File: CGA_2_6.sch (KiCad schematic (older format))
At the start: 11 parts, among them U24 74LS244, U32 74LS166, U33 27C256, U34 74LS273, U35 74LS273, U36 74LS244, U37 74LS374, U39 74LS174, U68 74LS86, U7 74LS166

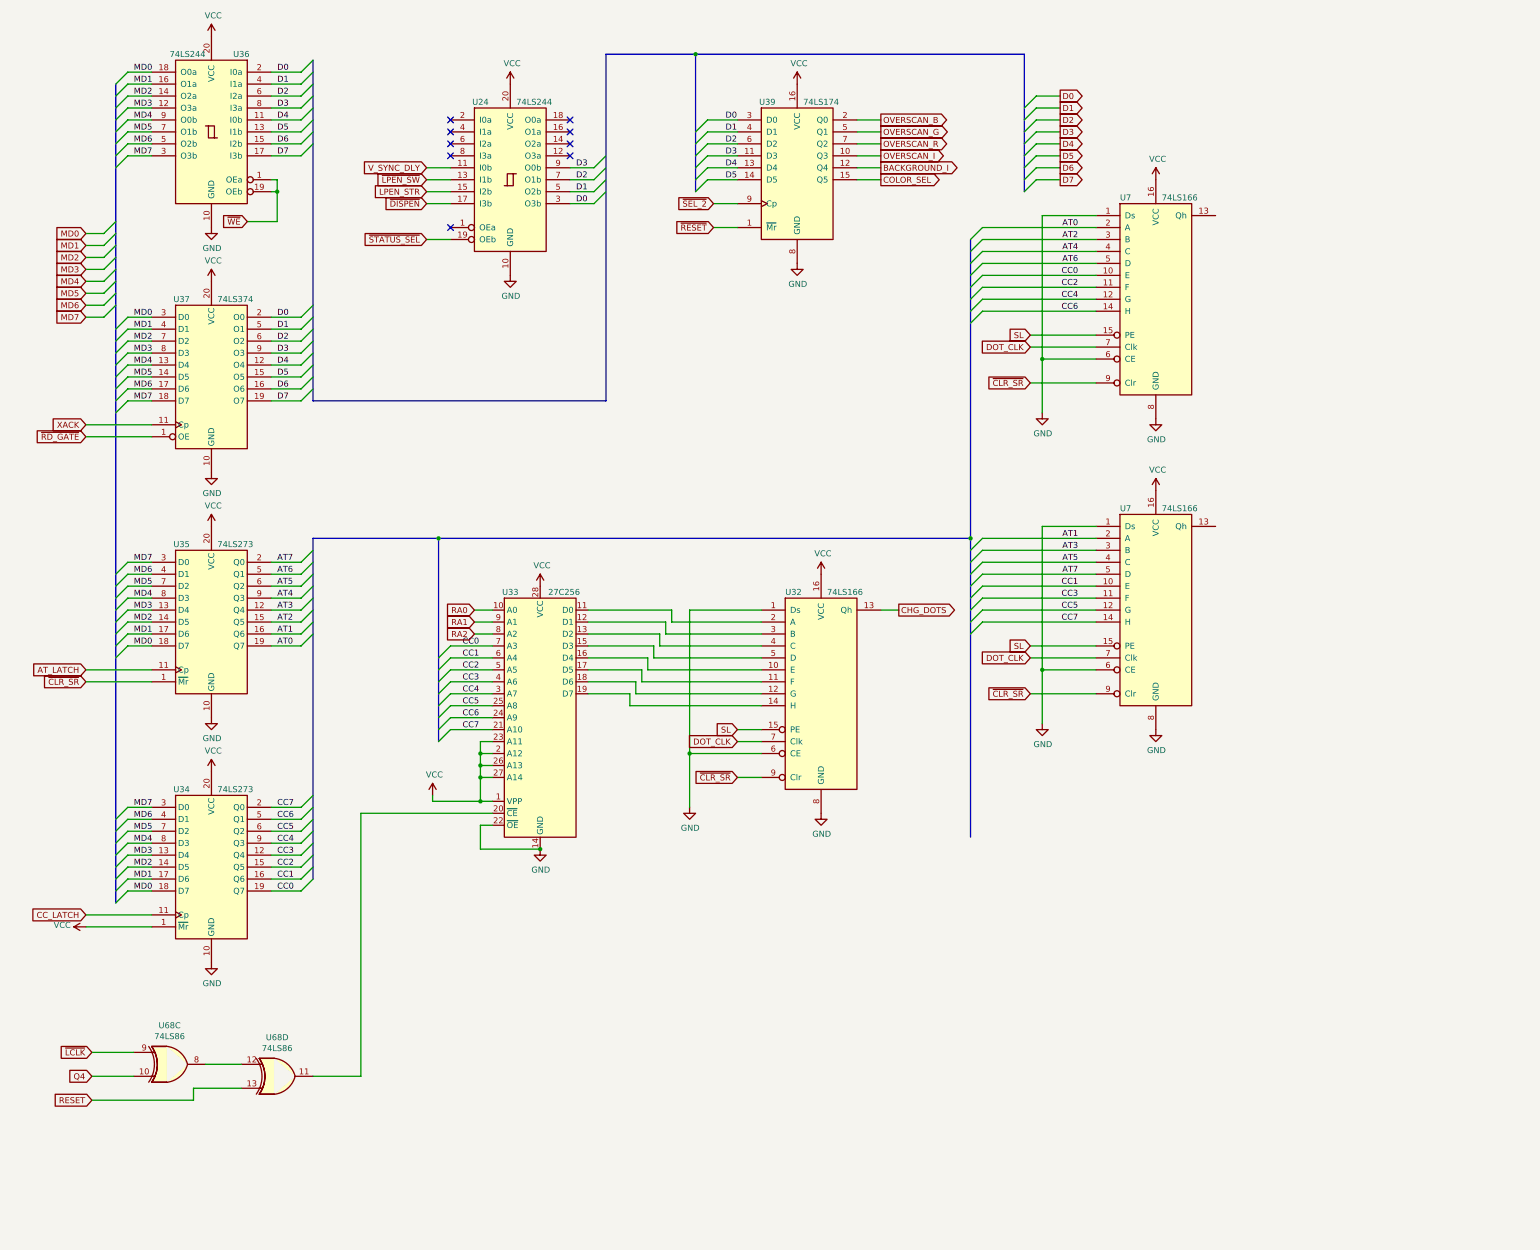
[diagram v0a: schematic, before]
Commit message: More of sheet 2
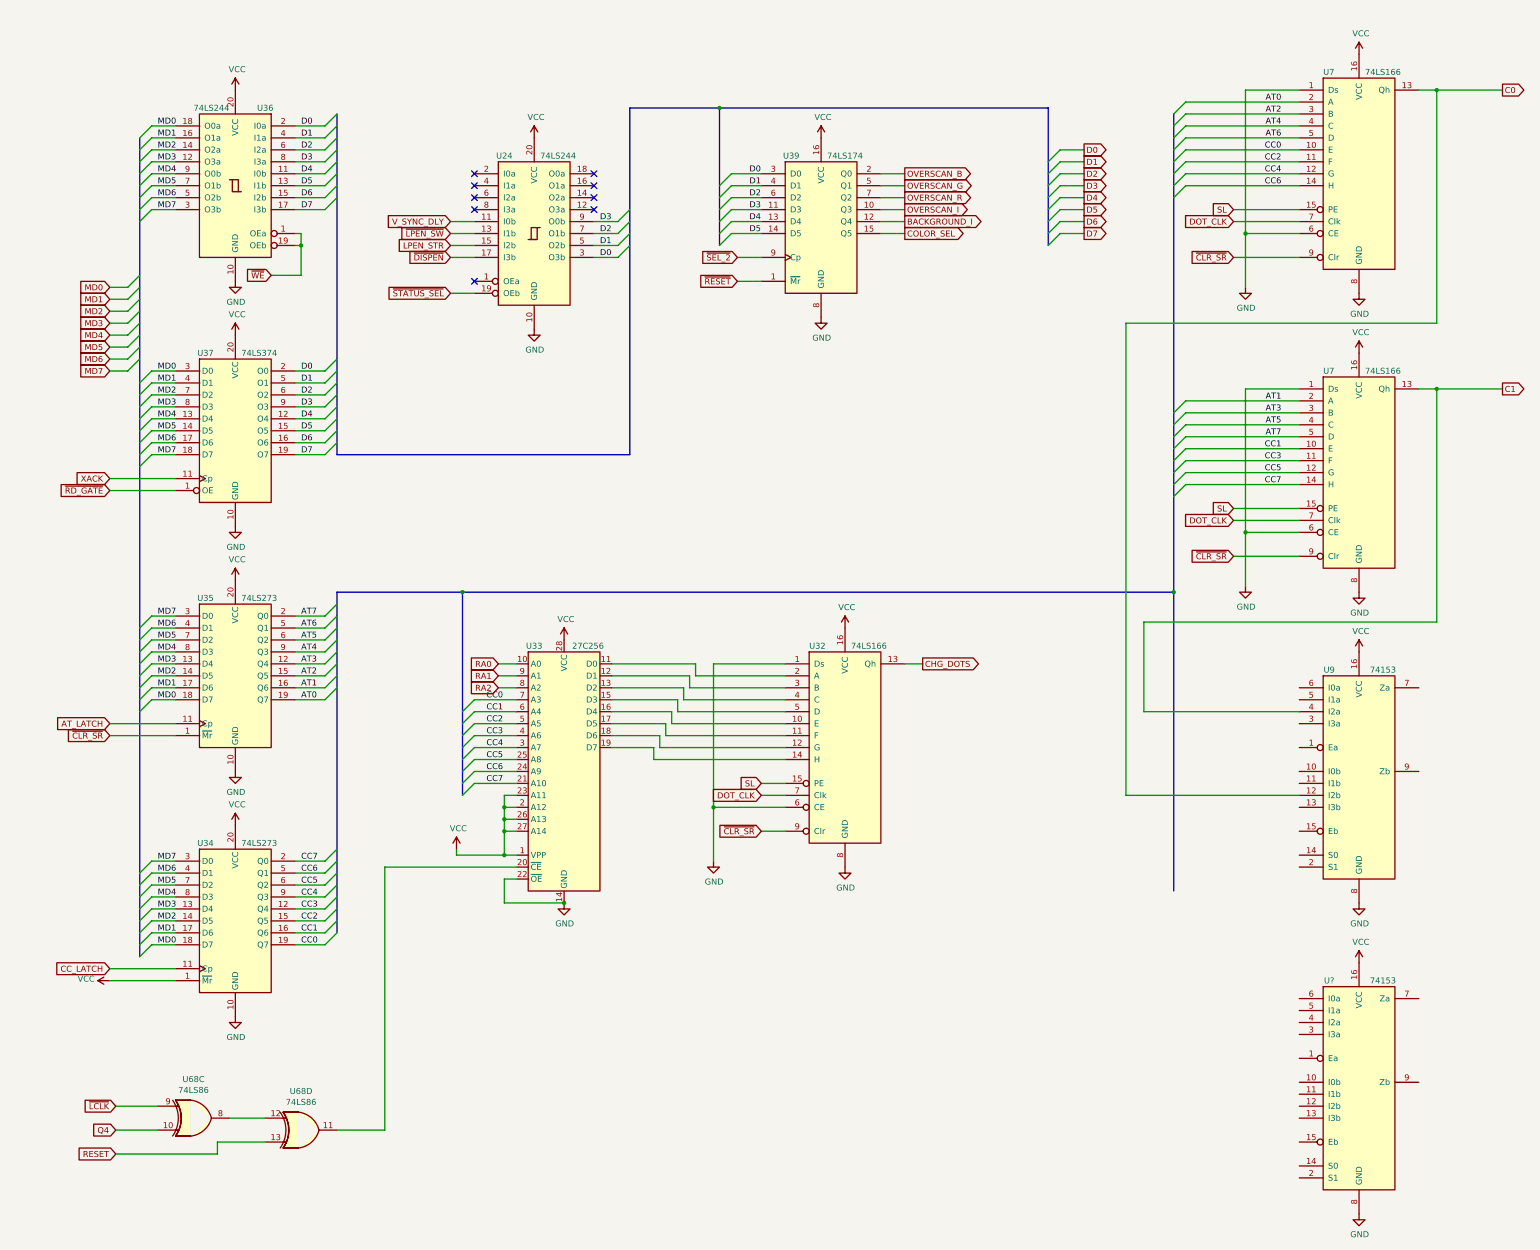
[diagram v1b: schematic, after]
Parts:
- added U9, U?: 74153, Package_DIP:DIP-16_W7.62mm_LongPads, symbol 74xx:74LS153
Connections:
- net GND: now also U9.8 (GND), U?.8 (GND)
- net VCC: now also U9.16 (VCC), U?.16 (VCC)
- net C0: now reaches U7.13 (Qh)
- net C0: now also U9.12 (I2b)
- net C1: now reaches U7.13 (Qh)
- net C1: now also U9.4 (I2a)
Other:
- moved on the sheet: U24, U32, U33, U34, U35, U36, U37, U39, U68C, U68D, U7

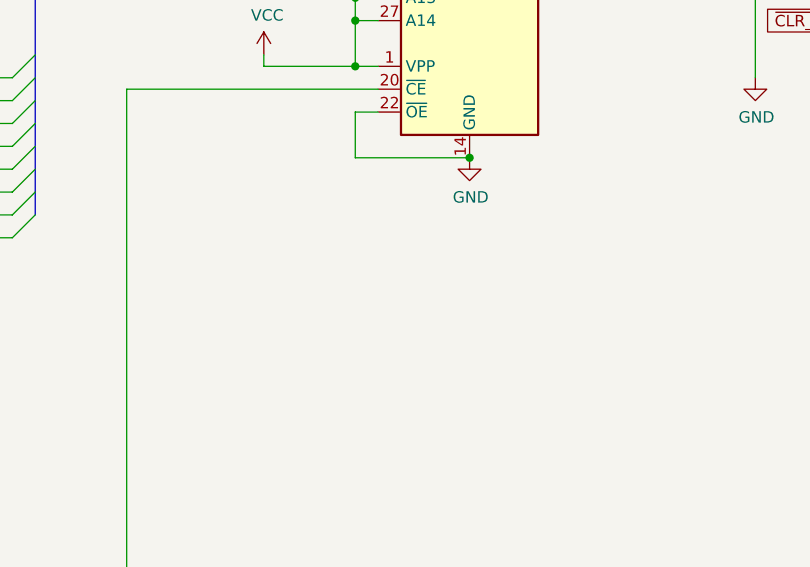
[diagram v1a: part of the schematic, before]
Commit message: Added MK36000 symbol
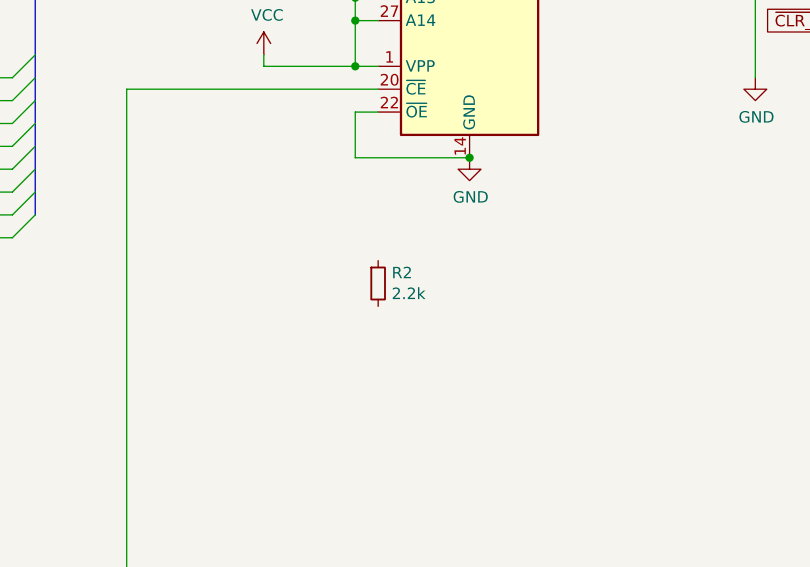
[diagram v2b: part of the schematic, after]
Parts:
- added R2: 2.2k, Resistor_THT:R_Axial_DIN0207_L6.3mm_D2.5mm_P10.16mm_Horizontal, symbol Device:R_Small
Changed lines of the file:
@@
 Wire Wire Line
 	12750 3950 13300 3950
+$Comp
+L Device:R_Small R2
+U 1 1 612D31E2
+P 5050 8800
+F 0 "R2" H 5109 8846 50  0000 L CNN
+F 1 "2.2k" H 5109 8755 50  0000 L CNN
+F 2 "Resistor_THT:R_Axial_DIN0207_L6.3mm_D2.5mm_P10.16mm_Horizontal" H 5050 8800 50  0001 C CNN
+F 3 "~" H 5050 8800 50  0001 C CNN
+	1    5050 8800
+	1    0    0    -1
+$EndComp
 $EndSCHEMATC

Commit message: More sheet 2
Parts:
- removed U33: 27C256, Package_DIP:DIP-28_W15.24mm_LongPads, symbol Memory_EPROM:27C256
- added U31: 74S08, Package_DIP:DIP-14_W7.62mm_LongPads, symbol 74xx:74LS08
- added U33: MK36000, Package_DIP:DIP-24_W15.24mm_LongPads, symbol ISA_CGA:MK36000
- gave numbers to parts that had none: 1
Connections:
- net AT0: now also U10.6 (I0a)
- net AT1: now also U9.10 (I0b)
- net AT2: now also U9.6 (I0a)
- net AT3: now also U10.10 (I0b)
- net AT4: now also U10.5 (I1a)
- net AT5: now also U9.11 (I1b)
- net AT6: now also U9.5 (I1a)
- net AT7: now also U31.9
- net CC0: now also U33.5 (A3)
- net CC1: now also U33.4 (A4)
- net CC2: now also U33.3 (A5)
- net CC3: now also U33.2 (A6)
- net CC4: now also U33.1 (A7)
- net CC5: now also U33.23 (A8)
- net CC6: now also U33.22 (A9)
- net CC7: now also U33.19 (A10)
- net GND: now also U33.12 (GND)
- net OVERSCAN_B: now also U10.3 (I3a)
- net OVERSCAN_G: now also U9.13 (I3b)
- net OVERSCAN_R: now also U9.3 (I3a)
- net RA0: now also U33.8 (A0)
- net RA1: now also U33.7 (A1)
- net RA2: now also U33.6 (A2)
- net VCC: now also R2.2, U33.21 (A12), U33.24 (VCC)
- net at U32.2 (A): now also U33.9 (D0)
- net at U32.3 (B): now also U33.10 (D1)
- net at U32.4 (C): now also U33.11 (D2)
- net at U32.5 (D): now also U33.13 (D3)
- net at U32.10 (E): now also U33.14 (D4)
- net at U32.11 (F): now also U33.15 (D5)
- net at U32.12 (G): now also U33.16 (D6)
- net at U32.14 (H): now also U33.17 (D7)
- net at U68.11: now also U33.20 (~CE)
- net STR: now reaches U9.1 (Ea)
- net STR: now also U10.1 (Ea), U10.15 (Eb), U9.15 (Eb)
- net MUX_A: now reaches U9.14 (S0)
- net MUX_A: now also U10.14 (S0)
- net MUX_B: now reaches U9.2 (S1)
- net MUX_B: now also U10.2 (S1)
- net at U10.11 (I1b): now also U31.8
- net SEL_BLUE: now reaches U10.4 (I2a)
- net at R2.1: now also U33.18 (A11)
- new net ~ENABLE_BLINK: U31.10
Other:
- moved on the sheet: R2

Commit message: More sheet 2
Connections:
- net BACKGROUND_I: now also U10.12 (I2b)
- net OVERSCAN_I: now also U10.13 (I3b)
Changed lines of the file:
@@
 Wire Wire Line
 	8950 9100 8150 9100
+Text GLabel 8150 9100 0    50   Input ~ 0
+~ENABLE_BLINK
+Wire Wire Line
+	11600 9950 10750 9950
+Wire Wire Line
+	10750 9950 10750 10050
+Wire Wire Line
+	10750 10050 9550 10050
+Text GLabel 9550 10050 0    50   Input ~ 0
+BACKGROUND_I
+Wire Wire Line
+	11600 10050 10850 10050
+Wire Wire Line
+	10850 10050 10850 10150
+Wire Wire Line
+	10850 10150 9550 10150
 Wire Bus Line
 	6000 1600 6000 4500
@@
 Wire Bus Line
 	1900 1850 1900 8700
-Text GLabel 8150 9100 0    50   Input ~ 0
-~ENABLE_BLINK
+Text GLabel 9550 10150 0    50   Input ~ 0
+OVERSCAN_I
 $EndSCHEMATC

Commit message: More sheet 2 changes
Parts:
- added U101: 74S174, Package_DIP:DIP-16_W7.62mm_LongPads, symbol 74xx:74LS174
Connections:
- net GND: now also U101.8 (GND)
- net VCC: now also U101.1 (~Mr), U101.16 (VCC)
- net ~RESET: now also U101.15 (Q5)
- net at U9.7 (Za): now also U101.3 (D0)
- net at U9.9 (Zb): now also U101.4 (D1)
- net at U10.7 (Za): now also U101.6 (D2)
- net at U10.9 (Zb): now also U101.11 (D3)
- new net: U101.12 (Q4), U101.14 (D5)
- new net B: U101.7 (Q2)
- new net G: U101.5 (Q1)
- new net I: U101.10 (Q3)
- new net R: U101.2 (Q0)
- new net ~14_MHZ: U101.9 (Cp)
- new net ~RESET': U101.13 (D4)
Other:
- moved on the sheet: R2, U10, U24, U31C, U32, U33, U34, U35, U36, U37, U39, U68C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
